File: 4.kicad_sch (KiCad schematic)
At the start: 1 part, among them U5 EPM570F100

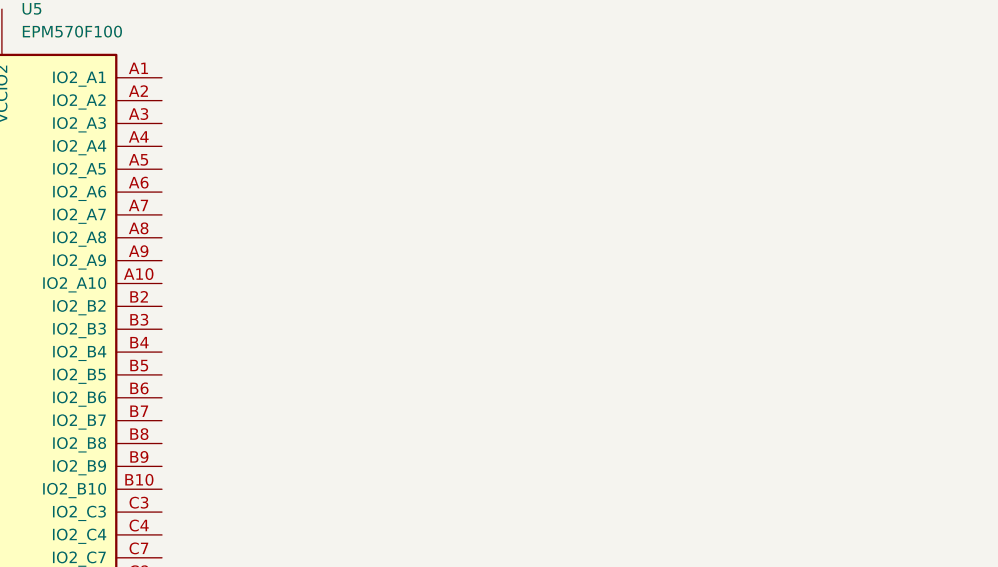
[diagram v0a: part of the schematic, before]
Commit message: open with 10
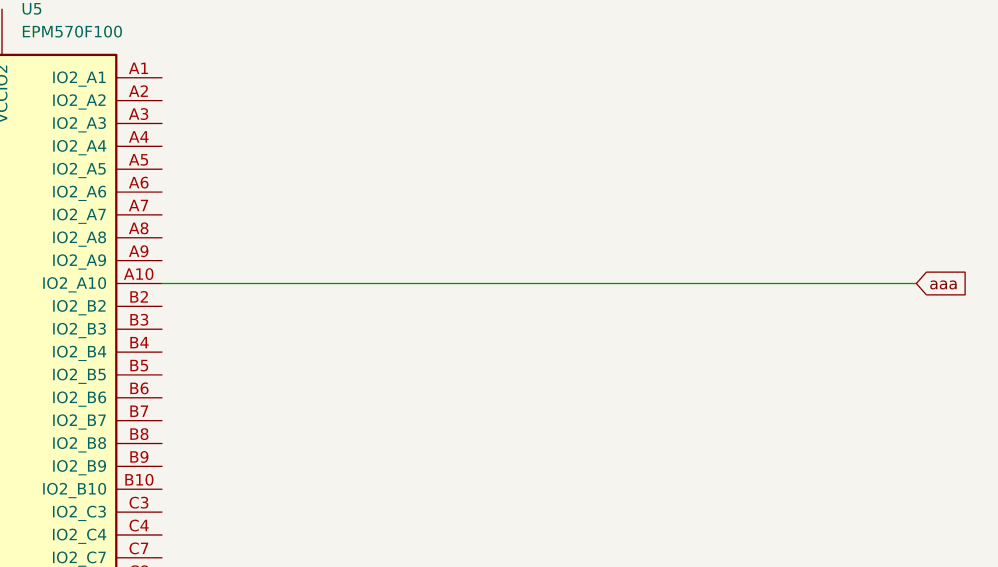
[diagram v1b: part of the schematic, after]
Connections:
- net aaa: now reaches U5.A10 (IO2_A10)
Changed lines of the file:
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@@
 (kicad_sch
-	(version 20250114)
+	(version 20260101)
 	(generator "eeschema")
-	(generator_version "9.0")
+	(generator_version "10.0")
 	(paper "A4")
+	(wire
+		(pts
+			(xy 109.22 81.28) (xy 193.04 81.28)
+		)
+		(stroke
+			(width 0)
+			(type default)
+		)
+	)
+	(global_label "aaa"
+		(shape input)
+		(at 193.04 81.28 0)
+		(fields_autoplaced yes)
+		(effects
+			(font
+				(size 1.27 1.27)
+			)
+			(justify left)
+		)
+		(property "Intersheetrefs" "${INTERSHEET_REFS}"
+			(at 199.4722 81.28 0)
+			(hide yes)
+			(show_name no)
+			(do_not_autoplace no)
+			(effects
+				(font
+					(size 1.27 1.27)
+				)
+				(justify left)
+			)
+		)
+	)
 	(symbol
 		(lib_id "CPLD_Altera:EPM570F100")
 		(at 81.28 109.22 0)
 		(unit 1)
+		(body_style 1)
 		(exclude_from_sim no)
 		(in_bom yes)
 		(on_board yes)
+		(in_pos_files yes)
 		(dnp no)
 		(fields_autoplaced yes)
 		(property "Reference" "U5"
 			(at 93.5833 50.8 0)
+			(show_name no)
+			(do_not_autoplace no)
 			(effects
 				(font
@@
 		(property "Value" "EPM570F100"
 			(at 93.5833 53.34 0)
+			(show_name no)
+			(do_not_autoplace no)
 			(effects
 				(font
@@
 		(property "Footprint" "Package_BGA:BGA-100_11.0x11.0mm_Layout10x10_P1.0mm_Ball0.5mm_Pad0.4mm_NSMD"
 			(at 93.98 166.37 0)
+			(hide yes)
+			(show_name no)
+			(do_not_autoplace no)
 			(effects
 				(font
@@
 				)
 				(justify left)
-				(hide yes)
 			)
 		)
 		(property "Datasheet" "https://www.altera.com/content/dam/altera-www/global/en_US/pdfs/literature/hb/max2/max2_mii5v1.pdf"
 			(at 81.28 109.22 0)
+			(hide yes)
+			(show_name no)
+			(do_not_autoplace no)
 			(effects
 				(font
 					(size 1.27 1.27)
 				)
-				(hide yes)
 			)
 		)
 		(property "Description" "Altera MAX2 CPLD with 570 LE"
 			(at 81.28 109.22 0)
+			(hide yes)
+			(show_name no)
+			(do_not_autoplace no)
 			(effects
 				(font
 					(size 1.27 1.27)
 				)
-				(hide yes)
 			)
 		)
